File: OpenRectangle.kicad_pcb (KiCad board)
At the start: 2 copper layers, 282.7 x 136.2 mm, 89 parts, among them J1 USB C Connector, J2 JTAG_TC2030, SW1 Boot, SW10 MX_SW_solder, SW11 MX_SW_HS, SW12 MX_SW_solder, SW13 MX_SW_HS, SW14 MX_SW_HS, SW15 MX_SW_solder, SW16 MX_SW_HS, SW17 MX_SW_solder, SW18 MX_SW_HS, SW19 MX_SW_solder, SW2 MX_SW_HS, SW20 MX_SW_solder, SW21 MX_SW_HS, SW22 MX_SW_HS, SW23 MX_SW_solder, SW24 MX_SW_HS, SW25 MX_SW_solder, SW26 MX_SW_HS, SW27 MX_SW_solder, SW28 MX_SW_HS, SW29 MX_SW_solder, SW3 MX_SW_solder, SW30 MX_SW_solder, SW31 MX_SW_HS, SW32 MX_SW_HS, SW33 MX_SW_solder, SW34 MX_SW_HS, SW35 MX_SW_solder, SW36 MX_SW_HS, SW37 MX_SW_solder, SW38 MX_SW_solder, SW39 MX_SW_HS, SW4 MX_SW_solder, SW40 MX_SW_HS, SW41 MX_SW_solder, SW5 MX_SW_HS, SW6 MX_SW_HS, SW7 MX_SW_solder, SW8 MX_SW_solder, SW9 MX_SW_HS, U1 XC6206, U2 USBLC6-2SC6, U3 RP2040, U4 W25Q128JVS, Y1 12MHz

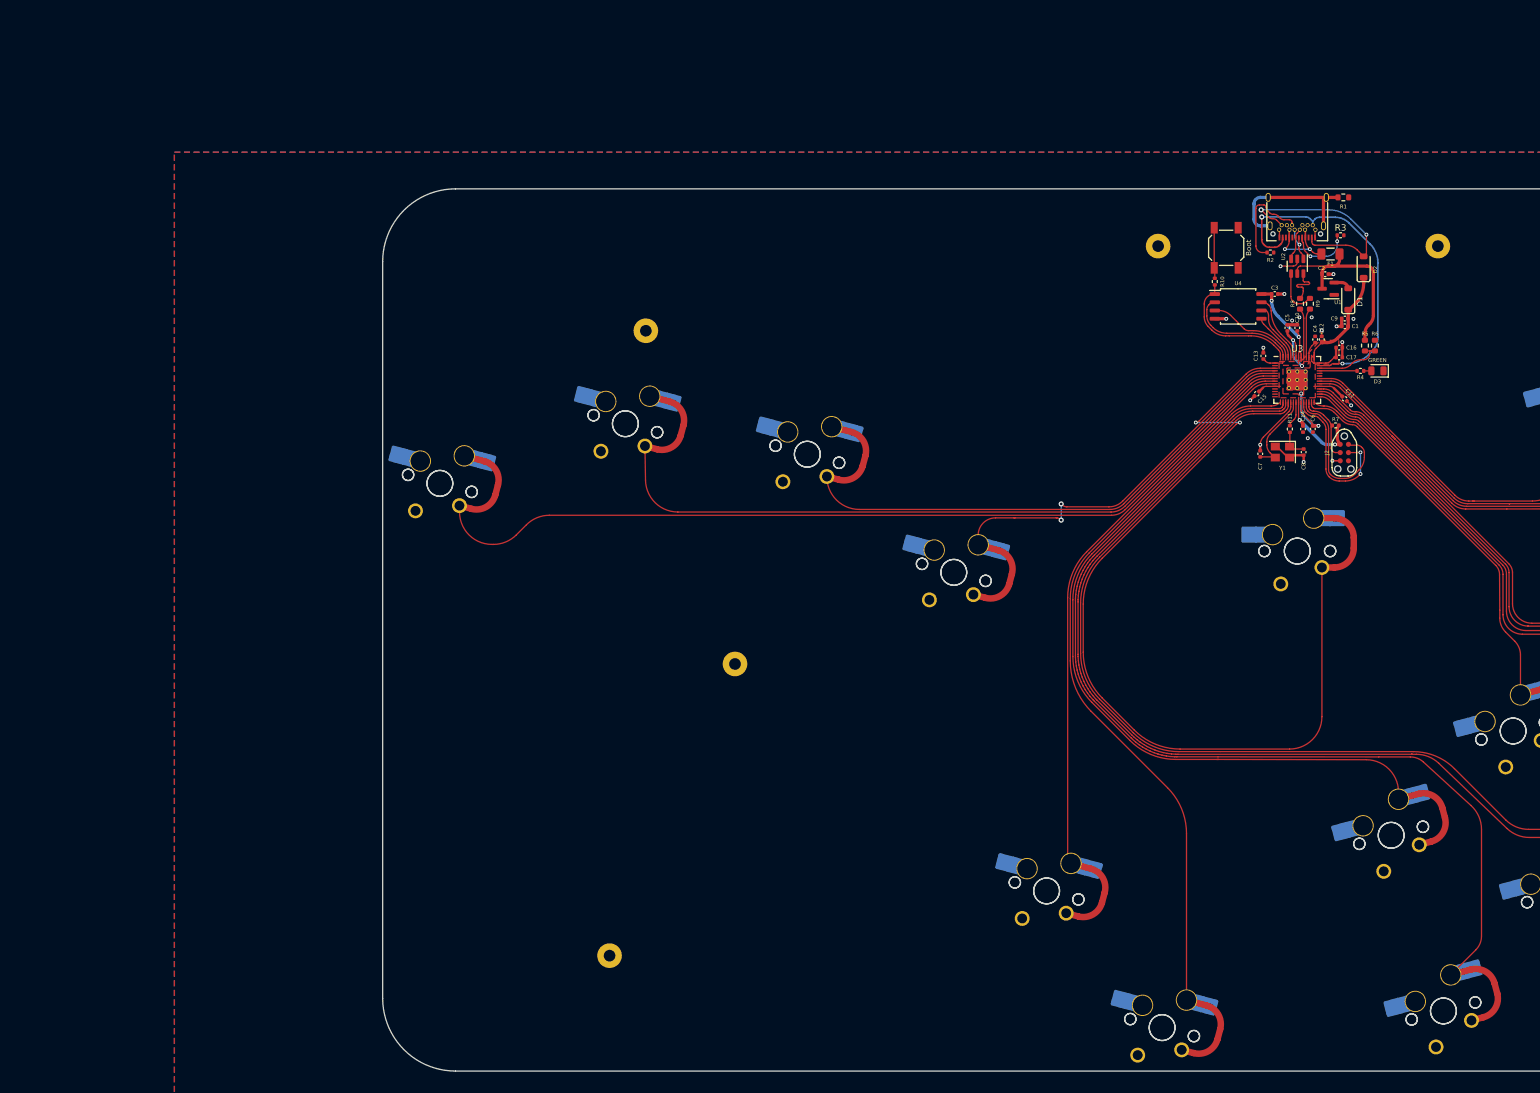
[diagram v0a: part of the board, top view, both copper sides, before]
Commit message: Added optional buttons
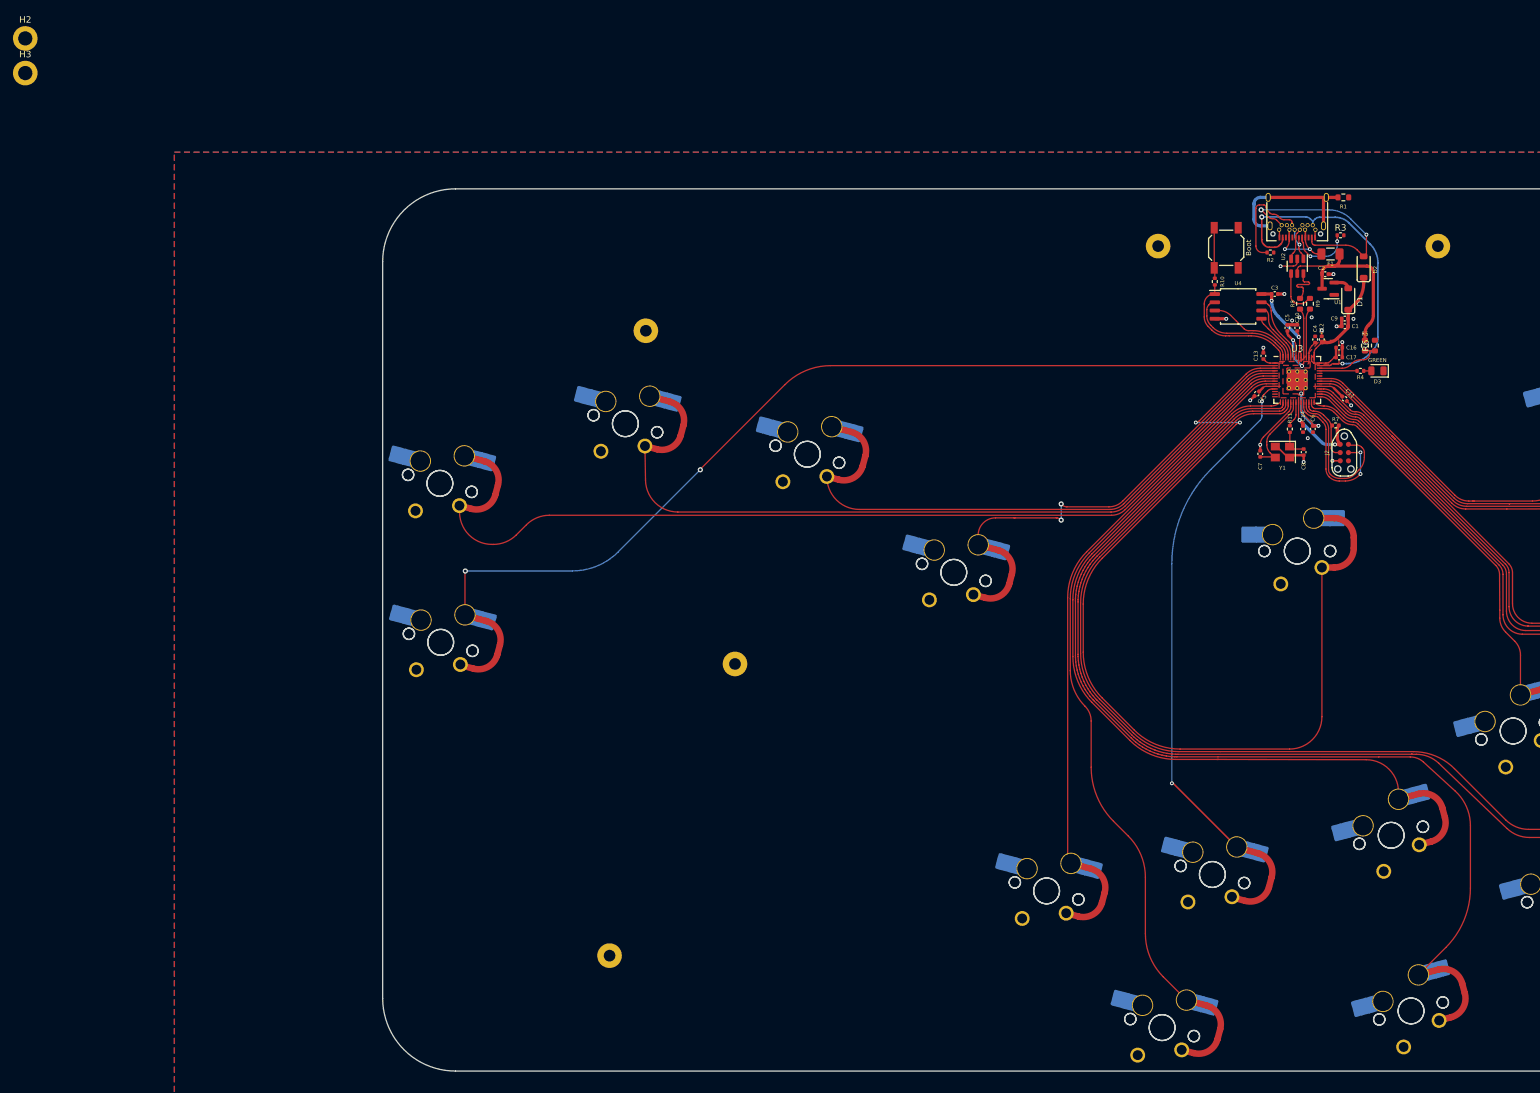
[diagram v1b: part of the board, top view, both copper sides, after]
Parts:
- added H2: MountingHole, MountingHole:MountingHole_2.2mm_M2_ISO14580_Pad, F.Cu at (2.17, 2.17)
- added H3: MountingHole, MountingHole:MountingHole_2.2mm_M2_ISO14580_Pad, F.Cu at (2.17, 7.53)
- added SW42: MX_SW_solder, marbastlib-mx:SW_MX_1u, F.Cu at (66.3, 95.4)
- added SW43: MX_SW_HS, marbastlib-mx:SW_MX_HS_1u, B.Cu at (66.3, 95.4)
- added SW44: MX_SW_HS, marbastlib-mx:SW_MX_HS_1u, B.Cu at (185.5, 131.3)
- added SW45: MX_SW_solder, marbastlib-mx:SW_MX_1u, F.Cu at (185.5, 131.3)
- moved SW36 5.00 mm to (216.1, 152.3)
- moved SW37 5.00 mm to (216.1, 152.3)
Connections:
- U3 pad 11: unconnected-(U3-GPIO8-Pad11) -> M3
- U3 pad 2: unconnected-(U3-GPIO0-Pad2) -> L2
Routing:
- net L2: track 0.00 -> 160.2 mm, vias 0 -> 2
- net M3: track 0.00 -> 96.9 mm, vias 0 -> 2
- net M2: track 131.5 -> 130.5 mm

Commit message: updated pinout to default haybox and revised case
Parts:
- removed H2, H3: MountingHole, MountingHole:MountingHole_2.2mm_M2_ISO14580_Pad
- moved D3 5.53 mm to (216.5, 53.4)
- moved R4 5.53 mm to (213.9, 53.4)
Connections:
- U3 pad 15: C_LT -> C_UP
- U3 pad 16: C_DN -> C_LT
- U3 pad 18: C_RT -> C_DN
- U3 pad 2: L2 -> START
- U3 pad 27: C_UP -> C_RT
- U3 pad 29: Z -> MS
- U3 pad 3: START -> L2
- U3 pad 30: X -> Z
- U3 pad 31: B -> LS
- U3 pad 32: MS -> X
- U3 pad 34: LS -> Y
- U3 pad 35: Y -> unconnected-(U3-GPIO23-Pad35)
- U3 pad 36: R -> VBUS_SENSE
- U3 pad 37: unconnected-(U3-GPIO25-Pad37) -> PICO_LED
- U3 pad 38: unconnected-(U3-GPIO26/ADC0-Pad38) -> B
- U3 pad 39: PICO_LED -> R
- U3 pad 40: VBUS_SENSE -> DATA
- U3 pad 41: DATA -> unconnected-(U3-GPIO29/ADC3-Pad41)
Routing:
- net C_RT: track 185.9 -> 98.3 mm
- net C_UP: track 76.1 -> 152.8 mm, vias 0 -> 2
- net LS: track 136.3 -> 164.3 mm
- net X: track 121.6 -> 100.3 mm
- net MS: track 163.3 -> 182.7 mm
- net B: track 90.7 -> 74.9 mm, vias 0 -> 2
- net START: track 153.6 -> 145.8 mm
- net PICO_LED: track 5.81 -> 12.2 mm, vias 0 -> 2
- net C_DN: track 171.5 -> 177.8 mm, vias 0 -> 2
- net R: track 76.3 -> 78.7 mm
- net C_LT: track 133.3 -> 135.3 mm
- net Z: track 154.2 -> 152.6 mm
- net VBUS_SENSE: track 10.6 -> 12.0 mm, vias 0 -> 2
